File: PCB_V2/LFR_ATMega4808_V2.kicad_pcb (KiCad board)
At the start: 2 copper layers, 70.5 x 90 mm, 74 parts, among them J1 Conn_02x02_Odd_Even, J10 Conn_01x03, J11 Conn_01x03, J2 Conn_02x05_Odd_Even, J5 Conn_01x03, J6 Conn_02x03_Odd_Even, J7 Conn_02x02_Odd_Even, J8 Conn_01x03, J9 Conn_01x03, M1 TestPoint, M2 TestPoint, M3 TestPoint, M4 TestPoint, Q1 PMOS, Q2 NMOS, Q3 NMOS, Q4 NMOS, Q5 NMOS, Q6 PMOS, Q7 NMOS, Q8 NMOS, U1 ATmega4808-A, U5 MCP1700x-330xxTO

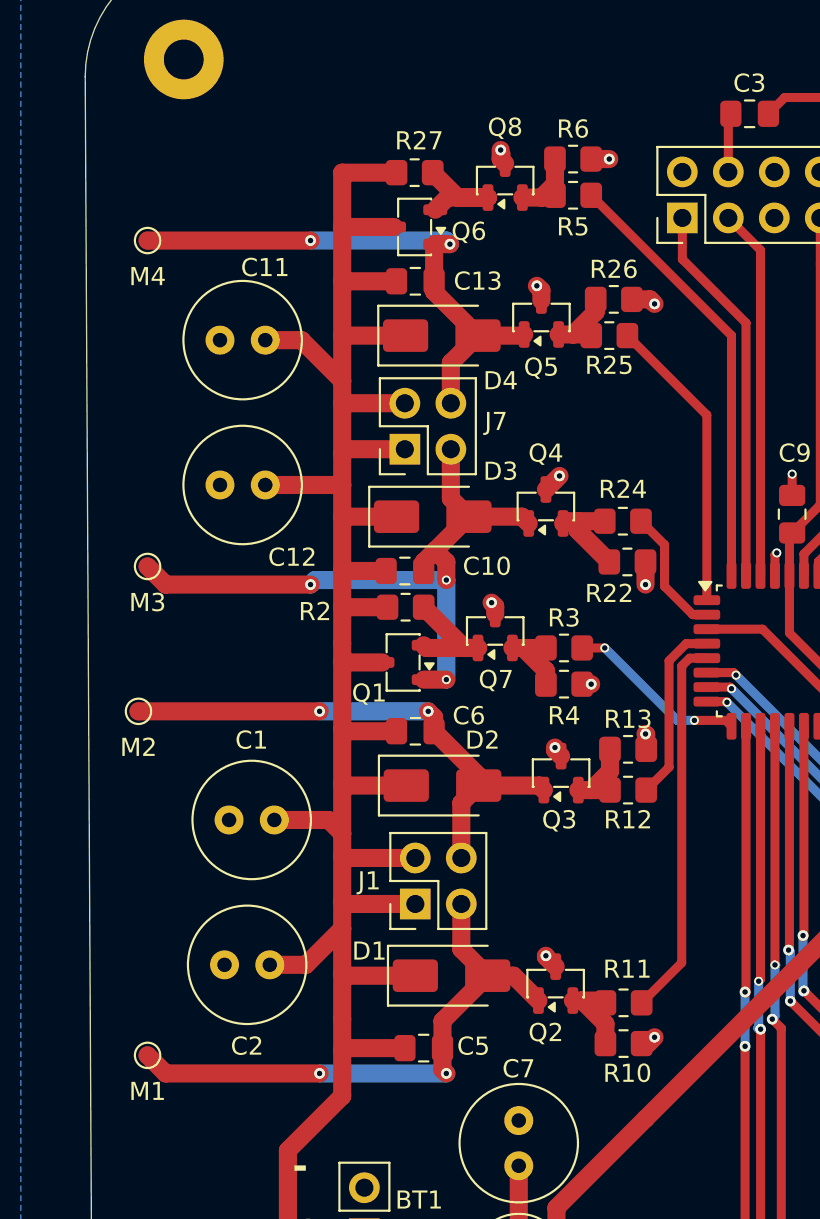
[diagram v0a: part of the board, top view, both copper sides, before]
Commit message: The transistor pins were wrong. Everything is adjusted and rewired
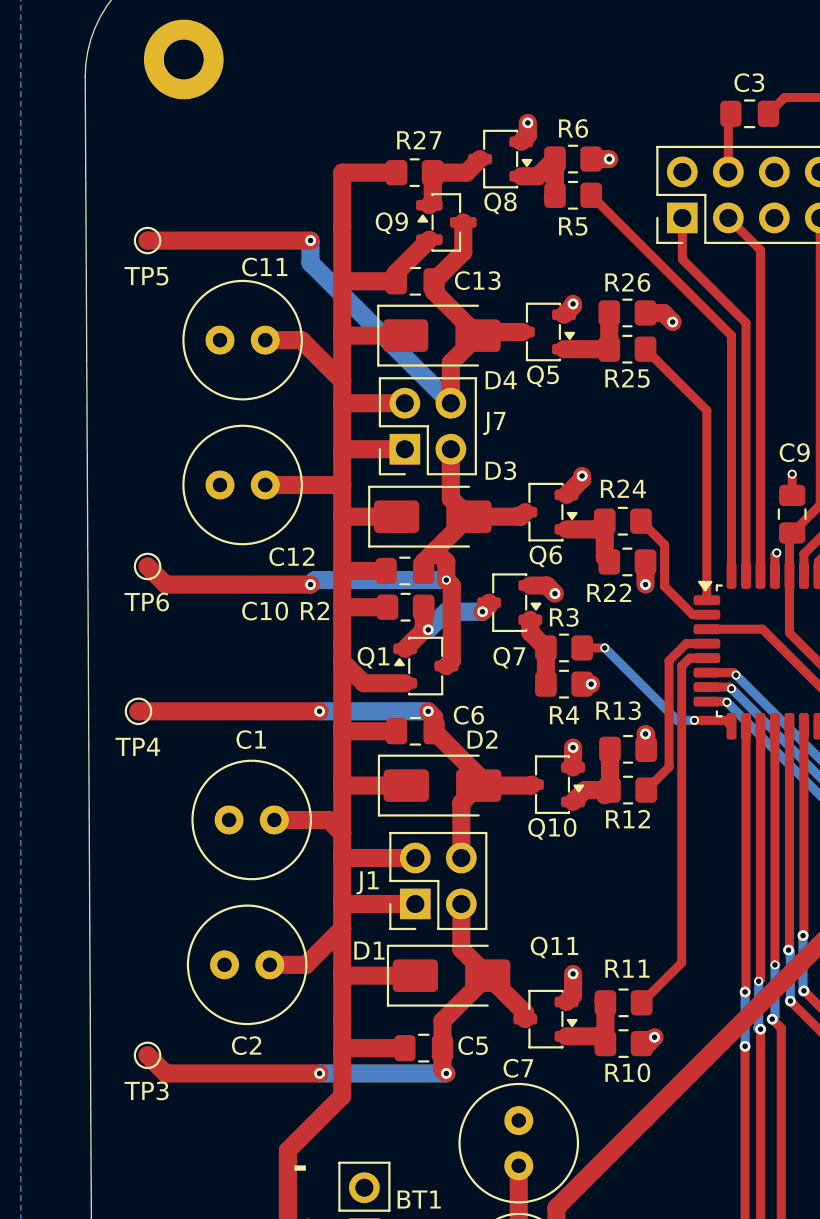
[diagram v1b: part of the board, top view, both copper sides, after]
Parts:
- removed Q2, Q3, Q4: NMOS, Package_TO_SOT_SMD:SOT-23
- added Q10: NMOS_BSR802NL6327HTSA1, Package_TO_SOT_SMD:SOT-23-3, F.Cu at (139.4, 118.0)
- added Q11: NMOS_BSR802NL6327HTSA1, Package_TO_SOT_SMD:SOT-23-3, F.Cu at (139.0, 131.0)
- added Q9: PMOS_Si2333DDS, Package_TO_SOT_SMD:SOT-23, F.Cu at (133.5, 87.0)
- Q1: value PMOS -> PMOS_Si2333DDS
- Q5, Q7, Q8: value NMOS -> NMOS_BSR802NL6327HTSA1; footprint Package_TO_SOT_SMD:SOT-23 -> Package_TO_SOT_SMD:SOT-23-3
- Q6: value PMOS -> NMOS_BSR802NL6327HTSA1
- R20: value 150 -> 2.2k
- moved Q6 17.3 mm to (139.0, 103.0)
- moved Q7 1.76 mm to (137.0, 108.0), turned to 180 degrees
- moved Q1 1.27 mm to (132.4, 111.5), turned to 0 degrees
- moved R25 1.25 mm to (143.5, 94.0)
- moved Q8 1.21 mm to (136.5, 83.5), turned to 180 degrees
- moved R26 1.06 mm to (143.5, 92.0)
- moved Q5 0.81 mm to (138.9, 93.0), turned to 180 degrees
- renumbered M1 to TP3, M2 to TP4, M4 to TP5, M3 to TP6
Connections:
- Q1 pad 1: Net-(D3-A) -> PMOS 1 In
- Q1 pad 2: PMOS 1 In -> +4.8V
- Q1 pad 3: +4.8V -> Net-(D3-A)
- Q5 pad 1: Net-(D4-A) -> Net-(Q5-G)
- Q5 pad 2: Net-(Q5-G) -> GND
- Q5 pad 3: GND -> Net-(D4-A)
- Q6 pad 1: Net-(D4-A) -> Net-(Q6-G)
- Q6 pad 2: PMOS 2 In -> GND
- Q6 pad 3: +4.8V -> Net-(D3-A)
- Q7 pad 1: PMOS 1 In -> Net-(Q7-G)
- Q7 pad 2: Net-(Q7-G) -> GND
- Q7 pad 3: GND -> PMOS 1 In
- Q8 pad 1: PMOS 2 In -> Net-(Q8-G)
- Q8 pad 2: Net-(Q8-G) -> GND
- Q8 pad 3: GND -> PMOS 2 In
- R22 pad 1: Net-(Q4-G) -> Net-(Q6-G)
- R24 pad 2: Net-(Q4-G) -> Net-(Q6-G)
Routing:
- net Net-(D4-A): track 30.6 -> 36.0 mm, vias 2 -> 1
- net Net-(Q4-G): track 5.33 -> 0.00 mm
- net Net-(Q6-G): track 0.00 -> 4.65 mm
- net GND: track 17.8 -> 20.9 mm
- net PMOS 2 In: track 6.81 -> 4.80 mm
- net Net-(D3-A): track 37.3 -> 35.3 mm, vias 3 -> 2
- net +4.8V: track 165.7 -> 167.6 mm
- net Motor 4: track 16.4 -> 15.3 mm
- net Net-(D2-A): track 29.4 -> 28.6 mm
- net Net-(Q10-G): track 4.43 -> 4.96 mm
- net PMOS 1 In: track 6.99 -> 6.79 mm, vias 0 -> 2

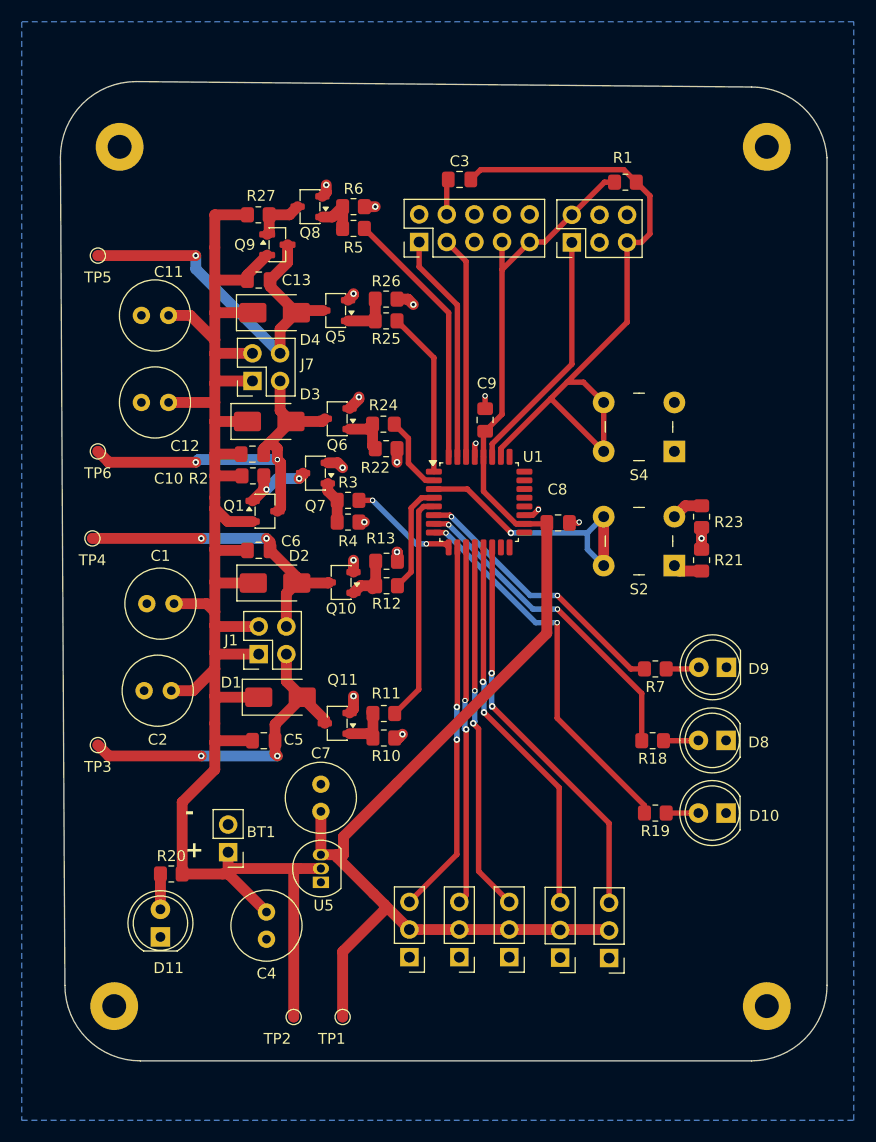
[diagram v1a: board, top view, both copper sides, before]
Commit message: fixing vias under pads, still not done
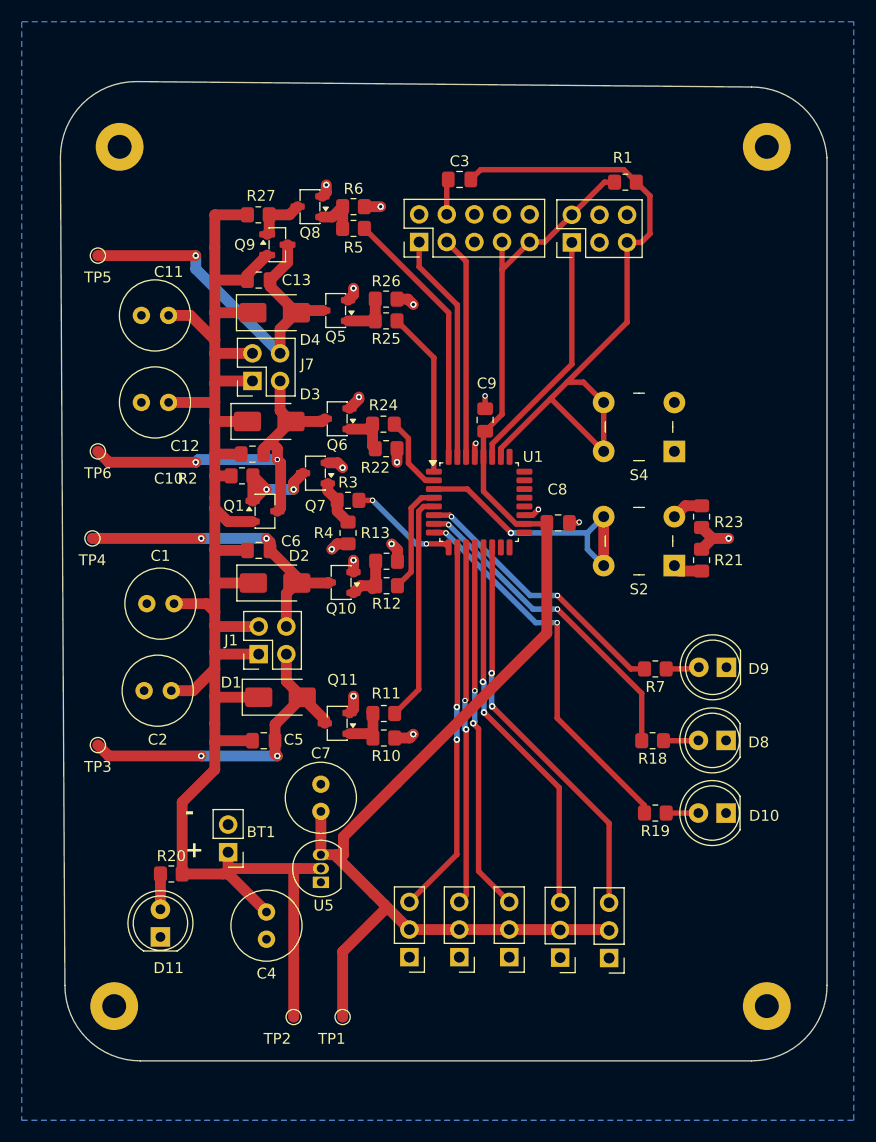
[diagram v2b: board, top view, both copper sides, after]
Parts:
- moved R2 1.00 mm to (130.2, 108.2)
- moved R4 1.00 mm to (140.0, 113.5), turned to -90 degrees
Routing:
- net GND: track 20.9 -> 27.4 mm
- net PMOS 1 In: track 6.79 -> 9.88 mm
- net +4.8V: track 167.6 -> 166.6 mm

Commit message: Fixes the vias
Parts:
- moved C8 1.28 mm to (160.0, 111.5), turned to -90 degrees
- moved C9 0.40 mm to (152.6, 102.7)
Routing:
- net +3.3V: track 128.6 -> 131.1 mm
- net GND: track 27.4 -> 29.2 mm
- net Net-(D3-A): track 35.3 -> 36.2 mm
- net Net-(D1-A): track 31.3 -> 30.6 mm

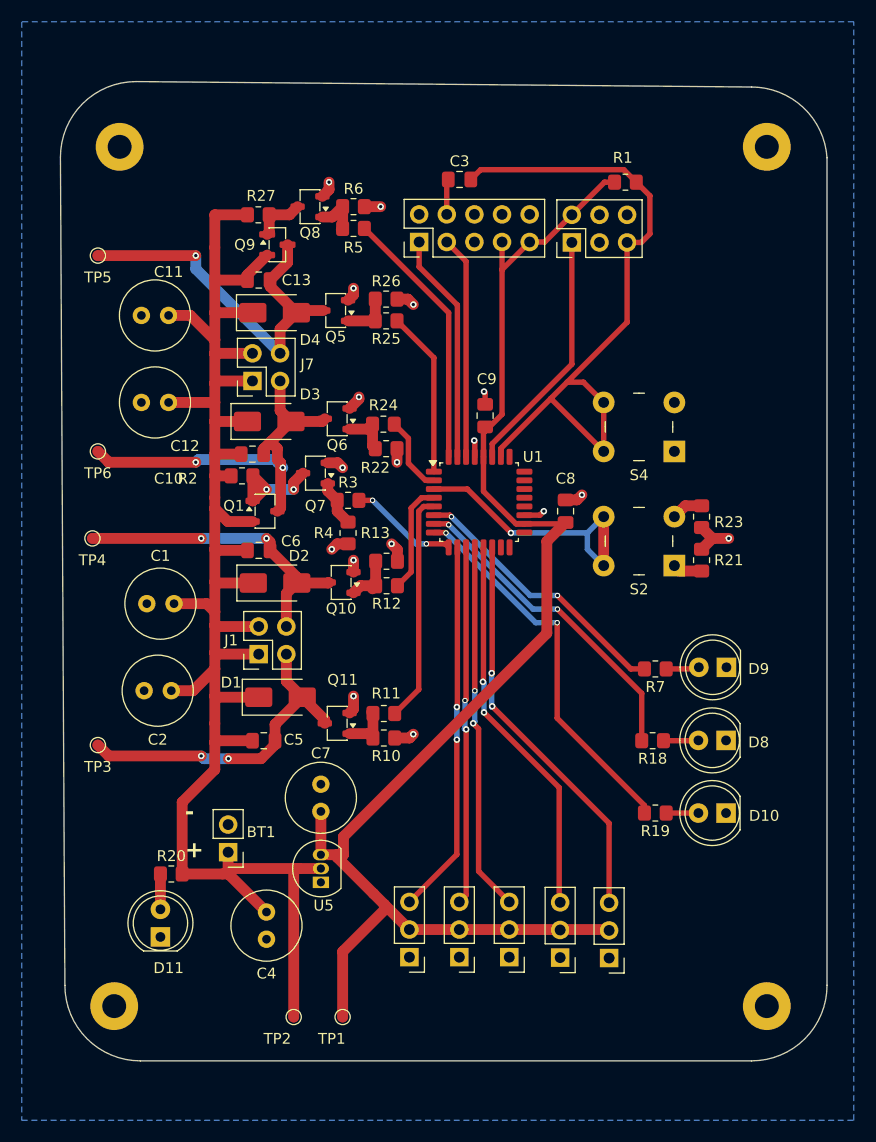
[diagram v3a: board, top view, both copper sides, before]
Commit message: Changed labels
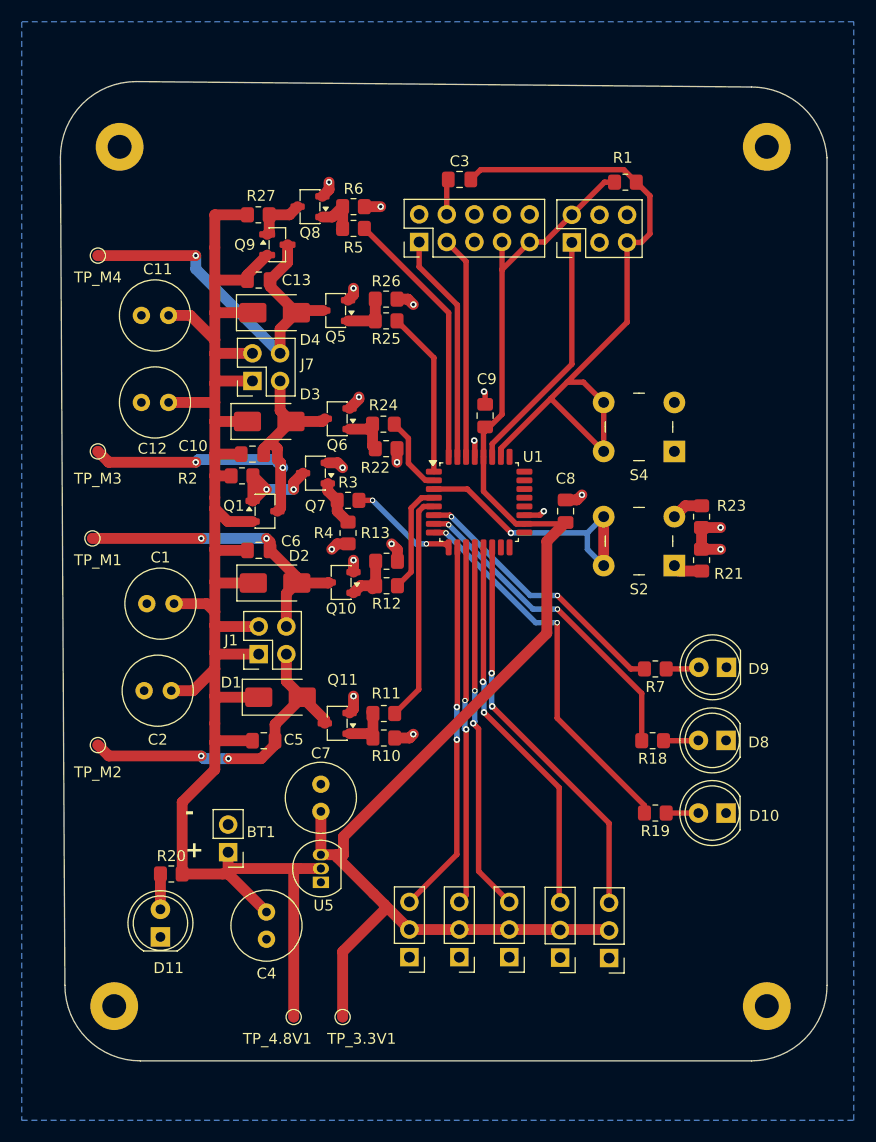
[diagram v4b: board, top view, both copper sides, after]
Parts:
- renumbered TP1 to TP_3.3V1, TP2 to TP_4.8V1, TP4 to TP_M1, TP3 to TP_M2, TP6 to TP_M3, TP5 to TP_M4
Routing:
- net GND: track 29.2 -> 30.4 mm, vias 17 -> 18
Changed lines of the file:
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@@
 		(descr "SMD pad as test Point, diameter 1.0mm")
 		(tags "test point SMD pad")
-		(property "Reference" "TP2"
+		(property "Reference" "TP_4.8V1"
 			(at -1.5 2 0)
 			(layer "F.SilkS")
@@
 		(tags "resistor handsolder")
 		(property "Reference" "R23"
-			(at 0.5 -2.5 180)
+			(at -1 -2.75 180)
 			(layer "F.SilkS")
 			(effects
@@
 		(descr "SMD pad as test Point, diameter 1.0mm")
 		(tags "test point SMD pad")
-		(property "Reference" "TP3"
-			(at 0 -2 0)
+		(property "Reference" "TP_M2"
+			(at 0 -2.5 0)
 			(layer "F.SilkS")
 			(effects
@@
 		(tags "C Radial series Radial pin pitch 2.50mm diameter 6.3mm height 5mm Non-Polar Electrolytic Capacitor")
 		(property "Reference" "C1"
-			(at 1.25 -4.4 0)
+			(at 1.25 -4.25 0)
 			(layer "F.SilkS")
 			(effects
@@
 		(descr "SMD pad as test Point, diameter 1.0mm")
 		(tags "test point SMD pad")
-		(property "Reference" "TP5"
+		(property "Reference" "TP_M4"
 			(at 0 -2 0)
 			(layer "F.SilkS")
@@
 		(descr "SMD pad as test Point, diameter 1.0mm")
 		(tags "test point SMD pad")
-		(property "Reference" "TP6"
-			(at 0 -2 0)
+		(property "Reference" "TP_M3"
+			(at 0 -2.5 0)
 			(layer "F.SilkS")
 			(effects
@@
 		(tags "resistor handsolder")
 		(property "Reference" "R21"
-			(at 0 2.5 180)
+			(at -1.25 2.5 180)
 			(layer "F.SilkS")
 			(effects
@@
 		(tags "capacitor handsolder")
 		(property "Reference" "C10"
-			(at -7.7125 2.25 0)
+			(at -5.4625 -0.75 0)
 			(layer "F.SilkS")
 			(effects
@@
 		(descr "SMD pad as test Point, diameter 1.0mm")
 		(tags "test point SMD pad")
-		(property "Reference" "TP1"
-			(at -1 2 0)
+		(property "Reference" "TP_3.3V1"
+			(at 1.75 2 0)
 			(layer "F.SilkS")
 			(effects
@@
 		(descr "SMD pad as test Point, diameter 1.0mm")
 		(tags "test point SMD pad")
-		(property "Reference" "TP4"
-			(at 0 -2 0)
+		(property "Reference" "TP_M1"
+			(at -0.5 -2 0)
 			(layer "F.SilkS")
 			(effects
@@
 		(tags "C Radial series Radial pin pitch 2.50mm diameter 6.3mm height 5mm Non-Polar Electrolytic Capacitor")
 		(property "Reference" "C12"
-			(at 4 4 0)
+			(at 1 4.25 0)
 			(layer "F.SilkS")
 			(effects
@@
 		(tags "C Radial series Radial pin pitch 2.50mm diameter 6.3mm height 5mm Non-Polar Electrolytic Capacitor")
 		(property "Reference" "C11"
-			(at 2.5 -4 0)
+			(at 1.5 -4.25 0)
 			(layer "F.SilkS")
 			(effects
@@
 	)
 	(segment
+		(start 172.5 113)
+		(end 174.25 113)
+		(width 1)
+		(layer "F.Cu")
+		(net "GND")
+	)
+	(segment
 		(start 137.6375 82.55)
 		(end 138.25 81.9375)
@@
 	)
 	(segment
-		(start 172.5 113)
-		(end 173.5 114)
-		(width 1)
-		(layer "F.Cu")
-		(net "GND")
-	)
-	(segment
 		(start 138.25 81.9375)
 		(end 138.25 81.25)
@@
 	)
 	(segment
+		(start 172.5 115)
+		(end 174.25 115)
+		(width 1)
+		(layer "F.Cu")
+		(net "GND")
+	)
+	(segment
 		(start 140.5 129.6875)
 		(end 140.5 128.5)
@@
 	)
 	(segment
-		(start 173.5 114)
-		(end 175 114)
-		(width 1)
-		(layer "F.Cu")
-		(net "GND")
-	)
-	(segment
 		(start 141.5 83.5)
 		(end 143 83.5)
@@
 	)
 	(segment
-		(start 172.5 115)
-		(end 173.5 114)
+		(start 140.5 91.6)
+		(end 140.5 91)
 		(width 1)
 		(layer "F.Cu")
@@
 	)
 	(segment
-		(start 140.5 91.6)
-		(end 140.5 91)
+		(start 144.5 105.75)
+		(end 144.5 107)
 		(width 1)
 		(layer "F.Cu")
@@
 	)
 	(segment
-		(start 144.5 105.75)
-		(end 144.5 107)
+		(start 172.5 115)
+		(end 172.5 113)
 		(width 1)
 		(layer "F.Cu")
@@
 	)
 	(via
+		(at 174.25 113)
+		(size 0.6)
+		(drill 0.3)
+		(layers "F.Cu" "B.Cu")
+		(net "GND")
+	)
+	(via
 		(at 152.5 100.5)
 		(size 0.6)
@@
 	)
 	(via
-		(at 175 114)
+		(at 139.5 107.5)
 		(size 0.6)
 		(drill 0.3)
@@
 	)
 	(via
-		(at 139.5 107.5)
+		(at 138.25 81.25)
 		(size 0.6)
 		(drill 0.3)
@@
 	)
 	(via
-		(at 138.25 81.25)
+		(at 151.6 105)
 		(size 0.6)
 		(drill 0.3)
@@
 	)
 	(via
-		(at 151.6 105)
+		(at 174.25 115)
 		(size 0.6)
 		(drill 0.3)
